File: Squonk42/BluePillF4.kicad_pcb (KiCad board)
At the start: 2 copper layers, 53.3 x 22.9 mm, 157 parts, among them J1 MH20-1, J2 MH20-1, J3 MH_RA4-1, J4 MR07C-06200, J5 47642-001, Q1 DMP2160UW-7, U1 AP2114HA-3.3TRG1, U2 AP2112K3.3-TRG1, U3 STM32F405RGT6, U4 SY6280, Y1 FC-135, Y2 NX3225GD

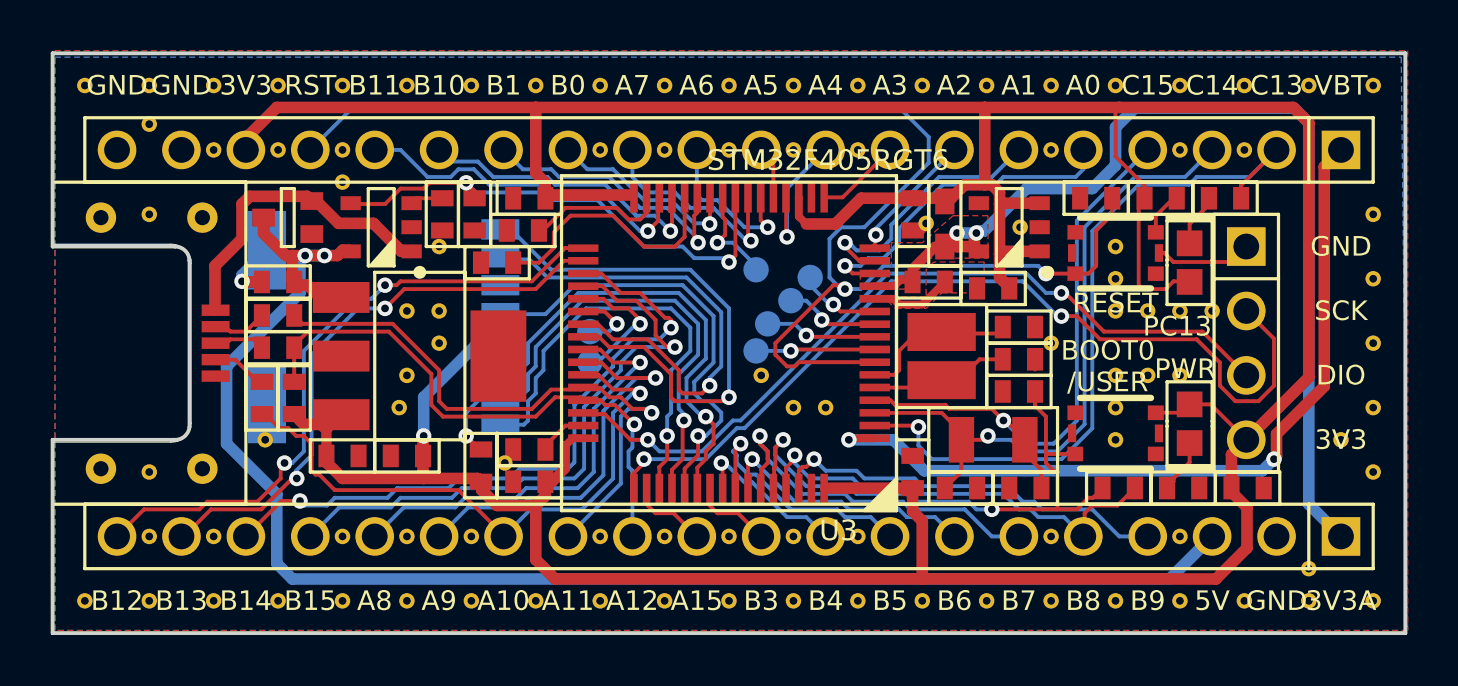
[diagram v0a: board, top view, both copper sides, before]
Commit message: Integrated changes from @racemaniac for fixing the edge layer issue Removed Ref/Value for U3 (STM32) on PCB top Fixed Top & Bottom GND zones minnimum width to 6 mils Added some missing GND tracks due to previous change  between thermal pads Fixed pads for J5 (micro USB) to be oval instead of round
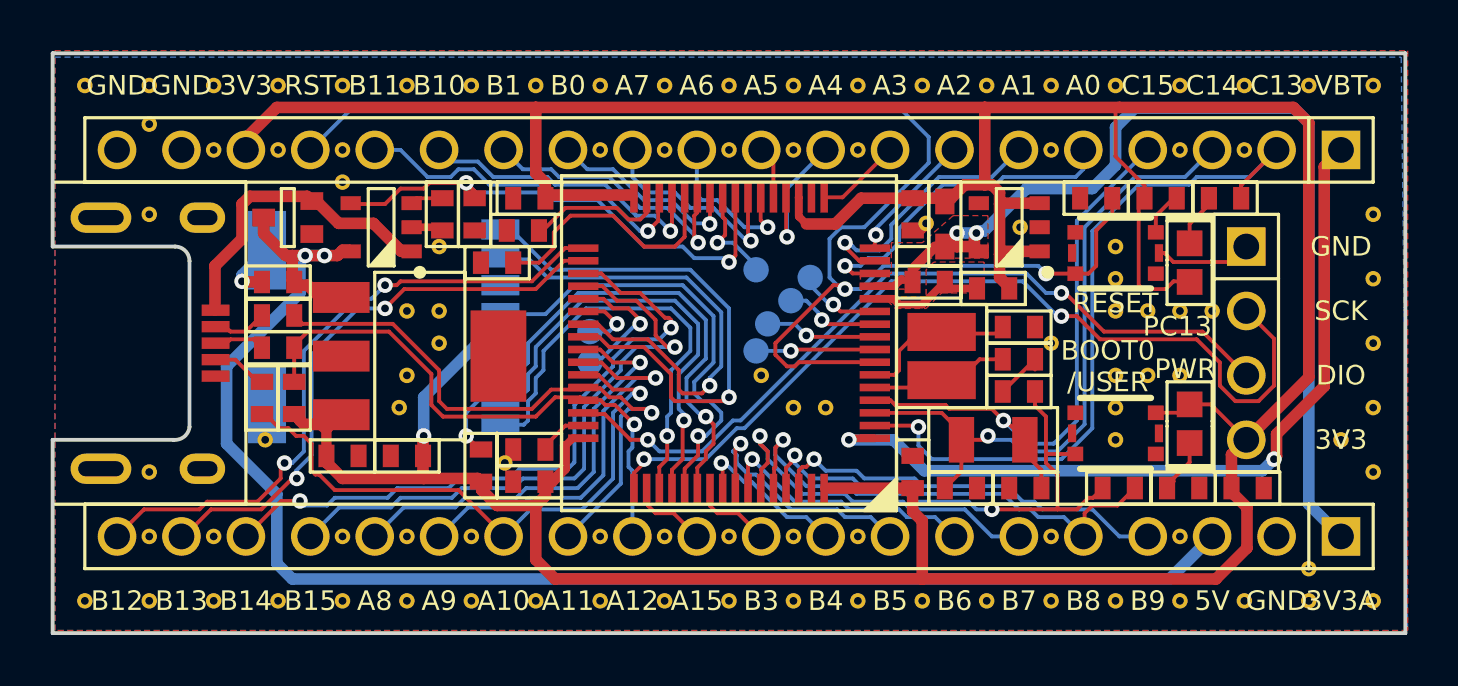
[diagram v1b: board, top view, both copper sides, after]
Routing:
- net GND: track 7.39 -> 11.1 mm
- net AGND: track 3.22 -> 4.60 mm
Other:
- outline, holes or cut-outs redrawn
- net class Power added: clearance 0.1523, trace_width 0.305, via_dia 0.6096, via_drill 0.3048

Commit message: Remove FET between VBus and +5V and replace with Schottky diode
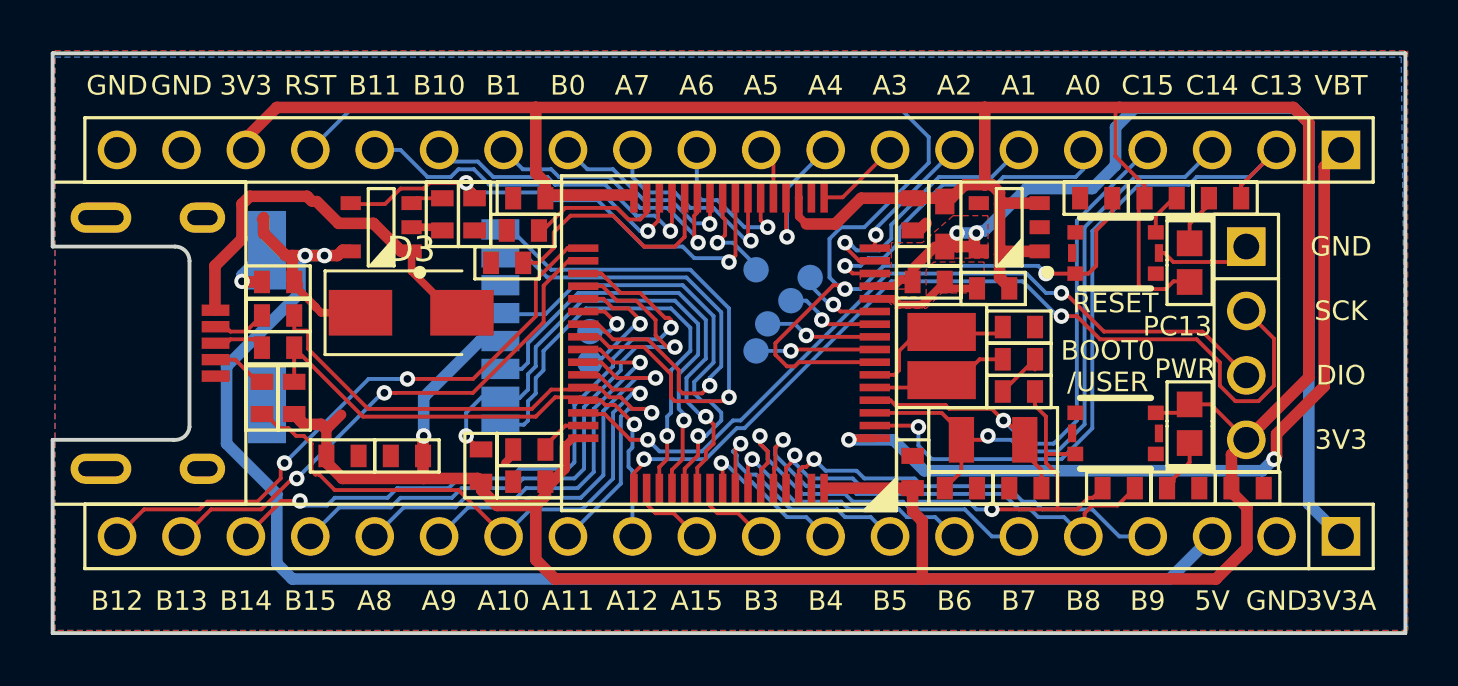
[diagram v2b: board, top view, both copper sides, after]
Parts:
- removed Q1: DMP2160UW-7, BluePillF4 Lib:SOT323
- removed REF** (x101): VIA_12MIL, BluePillF4 Lib:VIA_12MIL
- removed U$4: , OPEN_HARDWARE_LOGO
- removed U$6: , RECYCLE_BIN_LOGO
- removed U1: AP2114HA-3.3TRG1, BluePillF4 Lib:SOT223
- added D3: SS12, Diodes_SMD:D_SMA, F.Cu at (89.9, 59.9)
- moved R1 0.39 mm to (93.7, 57.9)
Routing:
- net /VBUS: track 12.4 -> 15.9 mm
- net /PB13: track 23.0 -> 21.3 mm
- net /PB12: track 25.7 -> 24.2 mm
- net /PA12: track 22.5 -> 21.2 mm
- net +5V: track 60.6 -> 61.9 mm

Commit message: Revert back to commit 7277910...
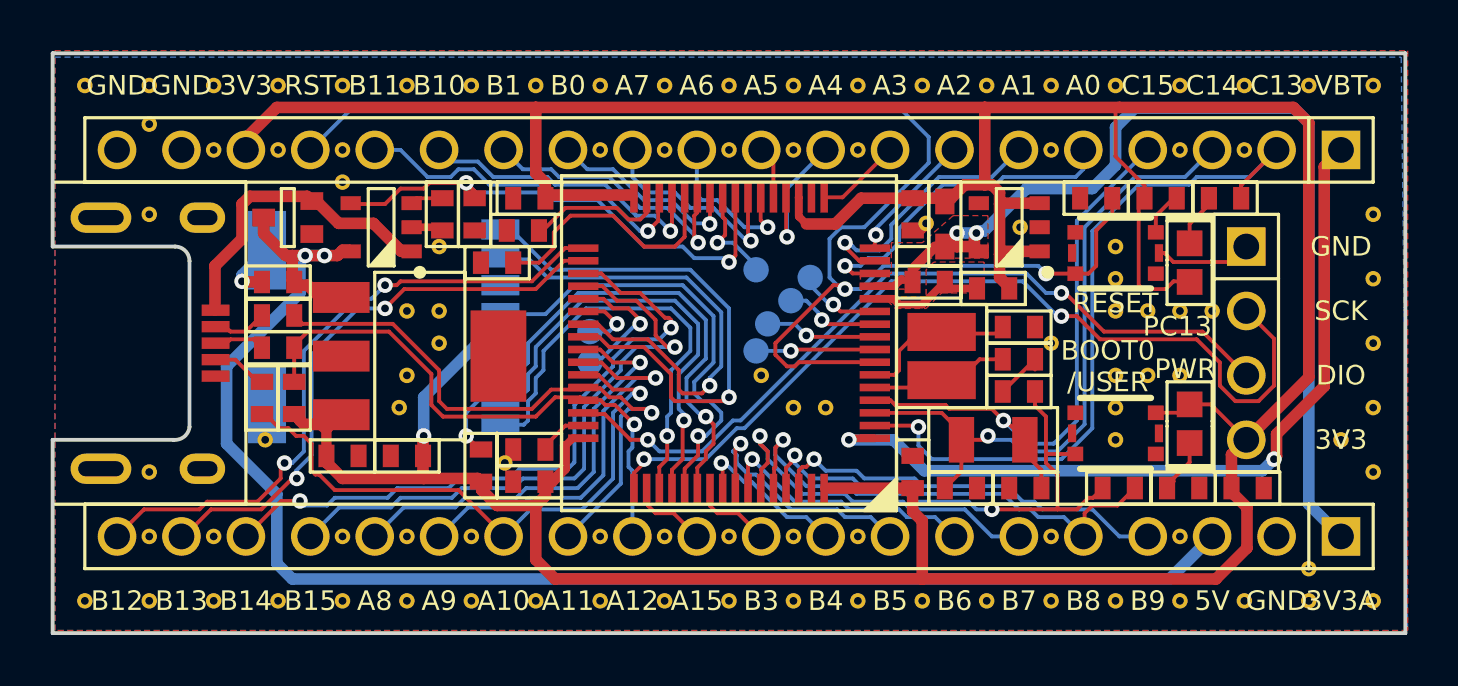
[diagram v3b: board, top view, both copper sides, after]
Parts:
- removed D3: SS12, Diodes_SMD:D_SMA
- added Q1: DMP2160UW-7, BluePillF4 Lib:SOT323, F.Cu at (85.0, 56.1)
- added REF**: VIA_12MIL, BluePillF4 Lib:VIA_12MIL, F.Cu at (77.0, 71.2)
- added REF**: VIA_12MIL, BluePillF4 Lib:VIA_12MIL, F.Cu at (99.9, 71.2)
- added REF**: VIA_12MIL, BluePillF4 Lib:VIA_12MIL, F.Cu at (93.6, 65.8)
- added REF**: VIA_12MIL, BluePillF4 Lib:VIA_12MIL, F.Cu at (113.9, 56.5)
- added REF**: VIA_12MIL, BluePillF4 Lib:VIA_12MIL, F.Cu at (102.4, 71.2)
- added REF**: VIA_12MIL, BluePillF4 Lib:VIA_12MIL, F.Cu at (104.9, 71.2)
- added REF**: VIA_12MIL, BluePillF4 Lib:VIA_12MIL, F.Cu at (107.5, 71.2)
- added REF**: VIA_12MIL, BluePillF4 Lib:VIA_12MIL, F.Cu at (110.0, 71.2)
- added REF**: VIA_12MIL, BluePillF4 Lib:VIA_12MIL, F.Cu at (112.6, 71.2)
- added REF**: VIA_12MIL, BluePillF4 Lib:VIA_12MIL, F.Cu at (115.1, 71.2)
- added REF**: VIA_12MIL, BluePillF4 Lib:VIA_12MIL, F.Cu at (117.6, 71.2)
- added REF**: VIA_12MIL, BluePillF4 Lib:VIA_12MIL, F.Cu at (120.2, 71.2)
- added REF**: VIA_12MIL, BluePillF4 Lib:VIA_12MIL, F.Cu at (122.7, 71.2)
- added REF**: VIA_12MIL, BluePillF4 Lib:VIA_12MIL, F.Cu at (79.5, 71.2)
- added REF**: VIA_12MIL, BluePillF4 Lib:VIA_12MIL, F.Cu at (125.3, 71.2)
- added REF**: VIA_12MIL, BluePillF4 Lib:VIA_12MIL, F.Cu at (127.8, 71.2)
- added REF**: VIA_12MIL, BluePillF4 Lib:VIA_12MIL, F.Cu at (79.5, 68.7)
- added REF**: VIA_12MIL, BluePillF4 Lib:VIA_12MIL, F.Cu at (82.1, 68.7)
- added REF**: VIA_12MIL, BluePillF4 Lib:VIA_12MIL, F.Cu at (87.2, 68.7)
- added REF**: VIA_12MIL, BluePillF4 Lib:VIA_12MIL, F.Cu at (89.7, 68.7)
- added REF**: VIA_12MIL, BluePillF4 Lib:VIA_12MIL, F.Cu at (92.2, 68.7)
- added REF**: VIA_12MIL, BluePillF4 Lib:VIA_12MIL, F.Cu at (97.3, 68.7)
- added REF**: VIA_12MIL, BluePillF4 Lib:VIA_12MIL, F.Cu at (99.9, 68.7)
- added REF**: VIA_12MIL, BluePillF4 Lib:VIA_12MIL, F.Cu at (102.4, 68.7)
- added REF**: VIA_12MIL, BluePillF4 Lib:VIA_12MIL, F.Cu at (82.1, 71.2)
- added REF**: VIA_12MIL, BluePillF4 Lib:VIA_12MIL, F.Cu at (104.9, 68.7)
- added REF**: VIA_12MIL, BluePillF4 Lib:VIA_12MIL, F.Cu at (107.5, 68.7)
- added REF**: VIA_12MIL, BluePillF4 Lib:VIA_12MIL, F.Cu at (115.1, 68.7)
- added REF**: VIA_12MIL, BluePillF4 Lib:VIA_12MIL, F.Cu at (120.2, 68.7)
- added REF**: VIA_12MIL, BluePillF4 Lib:VIA_12MIL, F.Cu at (125.3, 70.0)
- added REF**: VIA_12MIL, BluePillF4 Lib:VIA_12MIL, F.Cu at (127.8, 66.1)
- added REF**: VIA_12MIL, BluePillF4 Lib:VIA_12MIL, F.Cu at (126.5, 64.9)
- added REF**: VIA_12MIL, BluePillF4 Lib:VIA_12MIL, F.Cu at (127.8, 63.6)
- added REF**: VIA_12MIL, BluePillF4 Lib:VIA_12MIL, F.Cu at (127.8, 61.1)
- added REF**: VIA_12MIL, BluePillF4 Lib:VIA_12MIL, F.Cu at (127.8, 58.5)
- added REF**: VIA_12MIL, BluePillF4 Lib:VIA_12MIL, F.Cu at (84.6, 71.2)
- added REF**: VIA_12MIL, BluePillF4 Lib:VIA_12MIL, F.Cu at (127.8, 56.0)
- added REF**: VIA_12MIL, BluePillF4 Lib:VIA_12MIL, F.Cu at (122.7, 53.4)
- added REF**: VIA_12MIL, BluePillF4 Lib:VIA_12MIL, F.Cu at (120.2, 53.4)
- added REF**: VIA_12MIL, BluePillF4 Lib:VIA_12MIL, F.Cu at (115.1, 53.4)
- added REF**: VIA_12MIL, BluePillF4 Lib:VIA_12MIL, F.Cu at (107.5, 53.4)
- added REF**: VIA_12MIL, BluePillF4 Lib:VIA_12MIL, F.Cu at (104.9, 53.4)
- added REF**: VIA_12MIL, BluePillF4 Lib:VIA_12MIL, F.Cu at (102.4, 53.4)
- added REF**: VIA_12MIL, BluePillF4 Lib:VIA_12MIL, F.Cu at (99.9, 53.4)
- added REF**: VIA_12MIL, BluePillF4 Lib:VIA_12MIL, F.Cu at (97.3, 53.4)
- added REF**: VIA_12MIL, BluePillF4 Lib:VIA_12MIL, F.Cu at (87.2, 53.4)
- added REF**: VIA_12MIL, BluePillF4 Lib:VIA_12MIL, F.Cu at (87.2, 71.2)
- added REF**: VIA_12MIL, BluePillF4 Lib:VIA_12MIL, F.Cu at (84.6, 53.4)
- added REF**: VIA_12MIL, BluePillF4 Lib:VIA_12MIL, F.Cu at (82.1, 53.4)
- added REF**: VIA_12MIL, BluePillF4 Lib:VIA_12MIL, F.Cu at (79.5, 52.4)
- added REF**: VIA_12MIL, BluePillF4 Lib:VIA_12MIL, F.Cu at (79.5, 56.0)
- added REF**: VIA_12MIL, BluePillF4 Lib:VIA_12MIL, F.Cu at (89.7, 59.8)
- added REF**: VIA_12MIL, BluePillF4 Lib:VIA_12MIL, F.Cu at (91.0, 59.8)
- added REF**: VIA_12MIL, BluePillF4 Lib:VIA_12MIL, F.Cu at (91.0, 61.1)
- added REF**: VIA_12MIL, BluePillF4 Lib:VIA_12MIL, F.Cu at (89.7, 62.3)
- added REF**: VIA_12MIL, BluePillF4 Lib:VIA_12MIL, F.Cu at (77.0, 50.9)
- added REF**: VIA_12MIL, BluePillF4 Lib:VIA_12MIL, F.Cu at (79.5, 50.9)
- added REF**: VIA_12MIL, BluePillF4 Lib:VIA_12MIL, F.Cu at (89.7, 71.2)
- added REF**: VIA_12MIL, BluePillF4 Lib:VIA_12MIL, F.Cu at (82.1, 50.9)
- added REF**: VIA_12MIL, BluePillF4 Lib:VIA_12MIL, F.Cu at (84.6, 50.9)
- added REF**: VIA_12MIL, BluePillF4 Lib:VIA_12MIL, F.Cu at (87.2, 50.9)
- added REF**: VIA_12MIL, BluePillF4 Lib:VIA_12MIL, F.Cu at (89.7, 50.9)
- added REF**: VIA_12MIL, BluePillF4 Lib:VIA_12MIL, F.Cu at (92.2, 50.9)
- added REF**: VIA_12MIL, BluePillF4 Lib:VIA_12MIL, F.Cu at (94.8, 50.9)
- added REF**: VIA_12MIL, BluePillF4 Lib:VIA_12MIL, F.Cu at (97.3, 50.9)
- added REF**: VIA_12MIL, BluePillF4 Lib:VIA_12MIL, F.Cu at (99.9, 50.9)
- added REF**: VIA_12MIL, BluePillF4 Lib:VIA_12MIL, F.Cu at (102.4, 50.9)
- added REF**: VIA_12MIL, BluePillF4 Lib:VIA_12MIL, F.Cu at (104.9, 50.9)
- added REF**: VIA_12MIL, BluePillF4 Lib:VIA_12MIL, F.Cu at (92.2, 71.2)
- added REF**: VIA_12MIL, BluePillF4 Lib:VIA_12MIL, F.Cu at (107.5, 50.9)
- added REF**: VIA_12MIL, BluePillF4 Lib:VIA_12MIL, F.Cu at (110.0, 50.9)
- added REF**: VIA_12MIL, BluePillF4 Lib:VIA_12MIL, F.Cu at (112.6, 50.9)
- added REF**: VIA_12MIL, BluePillF4 Lib:VIA_12MIL, F.Cu at (115.1, 50.9)
- added REF**: VIA_12MIL, BluePillF4 Lib:VIA_12MIL, F.Cu at (117.6, 50.9)
- added REF**: VIA_12MIL, BluePillF4 Lib:VIA_12MIL, F.Cu at (120.2, 50.9)
- added REF**: VIA_12MIL, BluePillF4 Lib:VIA_12MIL, F.Cu at (122.7, 50.9)
- added REF**: VIA_12MIL, BluePillF4 Lib:VIA_12MIL, F.Cu at (125.3, 50.9)
- added REF**: VIA_12MIL, BluePillF4 Lib:VIA_12MIL, F.Cu at (127.8, 50.9)
- added REF**: VIA_12MIL, BluePillF4 Lib:VIA_12MIL, F.Cu at (103.7, 62.3)
- added REF**: VIA_12MIL, BluePillF4 Lib:VIA_12MIL, F.Cu at (94.8, 71.2)
- added REF**: VIA_12MIL, BluePillF4 Lib:VIA_12MIL, F.Cu at (104.9, 63.6)
- added REF**: VIA_12MIL, BluePillF4 Lib:VIA_12MIL, F.Cu at (106.2, 63.6)
- added REF**: VIA_12MIL, BluePillF4 Lib:VIA_12MIL, F.Cu at (121.5, 59.8)
- added REF**: VIA_12MIL, BluePillF4 Lib:VIA_12MIL, F.Cu at (120.2, 59.8)
- added REF**: VIA_12MIL, BluePillF4 Lib:VIA_12MIL, F.Cu at (118.9, 59.8)
- added REF**: VIA_12MIL, BluePillF4 Lib:VIA_12MIL, F.Cu at (117.6, 59.8)
- added REF**: VIA_12MIL, BluePillF4 Lib:VIA_12MIL, F.Cu at (117.6, 58.5)
- added REF**: VIA_12MIL, BluePillF4 Lib:VIA_12MIL, F.Cu at (117.6, 57.3)
- added REF**: VIA_12MIL, BluePillF4 Lib:VIA_12MIL, F.Cu at (120.2, 62.3)
- added REF**: VIA_12MIL, BluePillF4 Lib:VIA_12MIL, F.Cu at (118.9, 62.3)
- added REF**: VIA_12MIL, BluePillF4 Lib:VIA_12MIL, F.Cu at (97.3, 71.2)
- added REF**: VIA_12MIL, BluePillF4 Lib:VIA_12MIL, F.Cu at (117.6, 62.3)
- added REF**: VIA_12MIL, BluePillF4 Lib:VIA_12MIL, F.Cu at (117.6, 63.6)
- added REF**: VIA_12MIL, BluePillF4 Lib:VIA_12MIL, F.Cu at (117.6, 64.9)
- added REF**: VIA_12MIL, BluePillF4 Lib:VIA_12MIL, F.Cu at (115.1, 61.1)
- added REF**: VIA_12MIL, BluePillF4 Lib:VIA_12MIL, F.Cu at (91.0, 57.3)
- added REF**: VIA_12MIL, BluePillF4 Lib:VIA_12MIL, F.Cu at (87.2, 54.7)
- added REF**: VIA_12MIL, BluePillF4 Lib:VIA_12MIL, F.Cu at (79.5, 66.1)
- added REF**: VIA_12MIL, BluePillF4 Lib:VIA_12MIL, F.Cu at (89.4, 63.6)
- added REF**: VIA_12MIL, BluePillF4 Lib:VIA_12MIL, F.Cu at (84.1, 64.9)
- added REF**: VIA_12MIL, BluePillF4 Lib:VIA_12MIL, F.Cu at (110.2, 56.3)
- added U$4: , OPEN_HARDWARE_LOGO, B.Cu at (115.6, 61.8)
- added U$6: , RECYCLE_BIN_LOGO, B.Cu at (111.8, 65.6)
- added U1: AP2114HA-3.3TRG1, BluePillF4 Lib:SOT223, F.Cu at (90.2, 61.6)
- moved R1 0.39 mm to (93.3, 57.9)
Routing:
- net /VBUS: track 15.9 -> 12.4 mm
- net /PB13: track 21.3 -> 23.0 mm
- net /PB12: track 24.2 -> 25.7 mm
- net /PA12: track 21.2 -> 22.5 mm
- net +5V: track 61.9 -> 60.6 mm

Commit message: Powered AP2112 from +5V, not from +3.3V Added ferrite bead between GND and AGND Replaced 32kHz crystal by smaller FC-12M Adjusted solder mask clearance to 0 Made VBAT trace thinner Fixed MOSFET direction => replaced by an 1N5819HW Schottky diode Added PWR_FLAG to schematic to remove ERC warnings Replaced NC by real Kicad ones to remove ERC warnings Cleaned up Expansion connector labels in schematic Cleaned up traces for PA13-14 and PC13-15 Changed micro USB connector to BSC-Elec U02-BFD3111B0-009
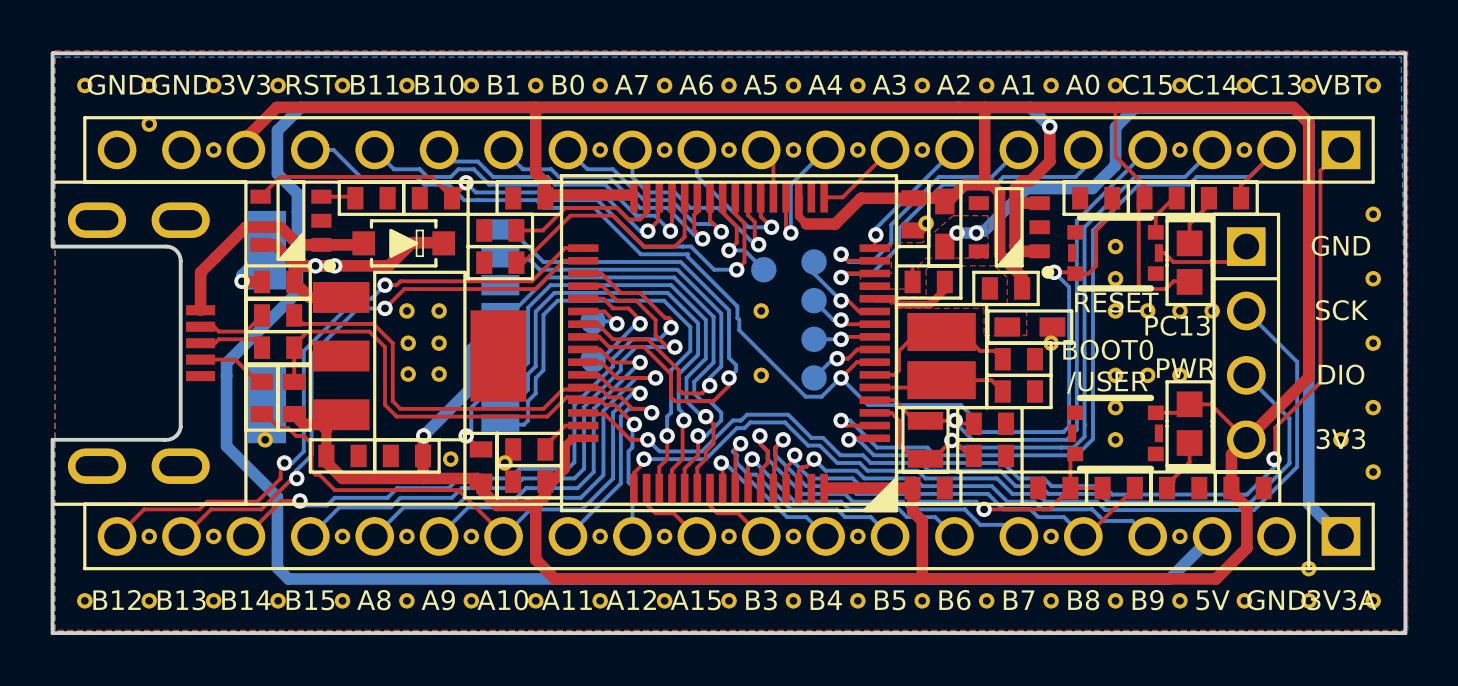
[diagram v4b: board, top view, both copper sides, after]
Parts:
- removed Q1: DMP2160UW-7, BluePillF4 Lib:SOT323
- removed U$4: , OPEN_HARDWARE_LOGO
- added D3: 1N5819HW, BluePillF4 Lib:SOD-123, F.Cu at (89.6, 57.1)
- added L2: BLM18BA470SN1D, BluePillF4 Lib:FB0603, F.Cu at (114.3, 60.4)
- added REF**: VIA_12MIL, BluePillF4 Lib:VIA_12MIL, F.Cu at (110.1, 53.4)
- added REF**: VIA_12MIL, BluePillF4 Lib:VIA_12MIL, F.Cu at (110.0, 53.4)
- J5: footprint BluePillF4 Lib:47662-001 -> BluePillF4 Lib:U02-BFD3111B0-009
- Y1: value FC-135 -> FC-12M; footprint BluePillF4 Lib:CRYSTAL_32X15 -> BluePillF4 Lib:FC-12M
- moved REF** 11.7 mm to (91.4, 65.6)
- moved REF** 5.03 mm to (91.0, 62.3)
- moved R4 4.06 mm to (115.2, 66.8)
- moved U4 3.57 mm to (85.1, 56.2)
- moved C3 2.90 mm to (112.7, 64.2), turned to 0 degrees
- moved R13 2.87 mm to (88.3, 55.3), turned to 0 degrees
- moved Y1 2.67 mm to (110.1, 64.9), turned to 90 degrees
- moved REF** 2.54 mm to (103.7, 59.8)
- moved PC0 2.52 mm to (105.8, 62.4)
- moved PC1 1.93 mm to (105.8, 60.9)
- moved REF** 1.80 mm to (103.7, 62.3)
- moved C2 1.71 mm to (112.7, 65.5)
- moved R7 1.65 mm to (90.8, 55.3), turned to 180 degrees
- moved REF** 1.37 mm to (89.8, 62.3)
- moved REF** 1.27 mm to (89.8, 61.1)
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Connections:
- U2 pad 1: +3V3 -> +5V
- U2 pad 3: +3V3 -> +5V
- Y1 pad 1: /PC15 -> /PC14
- Y1 pad 2: /PC14 -> /PC15
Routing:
- net +5V: track 60.6 -> 110.4 mm, vias 2 -> 3
- net /NRST: track 55.9 -> 48.6 mm
- net +3V3A: track 39.9 -> 34.5 mm
- net /BOOT0: track 23.2 -> 18.4 mm
- net /VBUS_EN: track 20.0 -> 24.7 mm
- net /PA13: track 31.3 -> 35.5 mm, vias 2 -> 1
- net /VBUS: track 12.4 -> 8.98 mm
- net +3V3: track 164.8 -> 161.8 mm
- net GND: track 11.1 -> 8.49 mm
- net /PC13: track 28.9 -> 31.5 mm
- net /PC15: track 24.2 -> 22.0 mm
- net /PC1: track 4.44 -> 2.44 mm
- net /PC0: track 4.71 -> 2.86 mm
- net /PA14: track 35.2 -> 36.8 mm, vias 2 -> 1
- net AGND: track 4.60 -> 3.40 mm
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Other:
- outline, holes or cut-outs redrawn
- rule pad_to_mask_clearance: 0.1524 -> 0
